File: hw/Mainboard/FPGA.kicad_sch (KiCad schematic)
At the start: 60 parts, among them J5 PMOD1, J6 PMOD2, J7 PROG, J8 FPGA_MCU, J9 BUS_EXPANSION, Q1 MMBT3904, SW3 CONFIG, U10 T8Q144C3

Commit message: hw: routing (wip)
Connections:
- net A2: now also U10.67 (GPIOB_RXP10); no longer U10.68 (GPIOB_RXN10)
- net I2C0_SCL: now also U10.15 (GPIOL_24_CLK0); no longer U10.14 (GPIOL_25_CLK1)
- net I2C0_SDA: now also U10.18 (GPIOL_20_CTRL0_CDI4); no longer U10.17 (GPIOL_21_CTRL1_CDI5)
- net I2C1_SCL: now also U10.14 (GPIOL_25_CLK1); no longer U10.15 (GPIOL_24_CLK0)
- net I2C1_SDA: now also U10.17 (GPIOL_21_CTRL1_CDI5); no longer U10.18 (GPIOL_20_CTRL0_CDI4)
- net RAM_A15: now also U10.68 (GPIOB_RXN10); no longer U10.67 (GPIOB_RXP10)
- net RDY: now also U10.43 (GPIOB_TXN04); no longer U10.45 (GPIOB_TXP06)
- net ~{SO}: now also U10.45 (GPIOB_TXP06); no longer U10.43 (GPIOB_TXN04)
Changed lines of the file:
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@@
     (effects (font (size 1.27 1.27)) (justify right bottom))
   )
-  (label "A2" (at 149.86 189.23 180)
-    (effects (font (size 1.27 1.27)) (justify right bottom))
+  (label "A2" (at 208.28 186.69 0)
+    (effects (font (size 1.27 1.27)) (justify left bottom))
   )
   (label "BE" (at 154.94 157.48 180)
@@
     (effects (font (size 1.27 1.27)) (justify left bottom))
   )
-  (label "RDY" (at 205.74 149.86 0)
-    (effects (font (size 1.27 1.27)) (justify left bottom))
+  (label "RDY" (at 154.94 152.4 180)
+    (effects (font (size 1.27 1.27)) (justify right bottom))
   )
   (label "A14" (at 389.89 93.98 0)
@@
     (effects (font (size 1.27 1.27)) (justify left bottom))
   )
-  (label "RAM_A15" (at 208.28 186.69 0)
-    (effects (font (size 1.27 1.27)) (justify left bottom))
+  (label "RAM_A15" (at 149.86 189.23 180)
+    (effects (font (size 1.27 1.27)) (justify right bottom))
   )
   (label "PMOD1_3" (at 311.15 2.54 180)
@@
     (effects (font (size 1.27 1.27)) (justify left bottom))
   )
-  (label "~{SO}" (at 154.94 152.4 180)
-    (effects (font (size 1.27 1.27)) (justify right bottom))
+  (label "~{SO}" (at 205.74 149.86 0)
+    (effects (font (size 1.27 1.27)) (justify left bottom))
   )
   (label "RAM_A11" (at 314.96 113.03 0)
@@
     (effects (font (size 1.27 1.27)) (justify right))
   )
-  (hierarchical_label "I2C1_SDA" (shape bidirectional) (at 149.86 127 180)
+  (hierarchical_label "I2C1_SDA" (shape bidirectional) (at 149.86 129.54 180)
     (effects (font (size 1.27 1.27)) (justify right))
   )
@@
     (effects (font (size 1.27 1.27)) (justify right))
   )
-  (hierarchical_label "I2C0_SDA" (shape bidirectional) (at 149.86 129.54 180)
+  (hierarchical_label "I2C0_SDA" (shape bidirectional) (at 149.86 127 180)
     (effects (font (size 1.27 1.27)) (justify right))
   )
@@
     (effects (font (size 1.27 1.27)) (justify right))
   )
-  (hierarchical_label "I2C0_SCL" (shape input) (at 210.82 127 0)
+  (hierarchical_label "I2C0_SCL" (shape input) (at 210.82 124.46 0)
     (effects (font (size 1.27 1.27)) (justify left))
   )
@@
     (effects (font (size 1.27 1.27)) (justify left))
   )
-  (hierarchical_label "I2C1_SCL" (shape input) (at 210.82 124.46 0)
-    (effects (font (size 1.27 1.27)) (justify left))
-  )
+  (hierarchical_label "I2C1_SCL" (shape input) (at 210.82 127 0)
+    (effects (font (size 1.27 1.27)) (justify left))
+  )

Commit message: hw: header_and_jumper, button for flashing (wip)
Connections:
- net GND: now also J8.14 (Pin_14)
- net PMOD2_1: now also U10.139 (GPIOL_68); no longer U10.138 (GPIOL_69_CBSEL1)
- net PMOD2_5: now also U10.138 (GPIOL_69_CBSEL1); no longer U10.139 (GPIOL_68)
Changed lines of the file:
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@@
     (stroke (width 0) (type default) (color 0 0 0 0))
   )
+  (wire (pts (xy 226.06 43.18) (xy 217.17 43.18))
+    (stroke (width 0) (type default) (color 0 0 0 0))
+  )
   (wire (pts (xy 95.25 160.02) (xy 95.25 162.56))
     (stroke (width 0) (type default) (color 0 0 0 0))
@@
     (stroke (width 0) (type default) (color 0 0 0 0))
   )
+  (wire (pts (xy 217.17 58.42) (xy 226.06 58.42))
+    (stroke (width 0) (type default) (color 0 0 0 0))
+  )
   (wire (pts (xy 53.34 29.21) (xy 55.88 29.21))
     (stroke (width 0) (type default) (color 0 0 0 0))
@@
     (effects (font (size 1.27 1.27)) (justify left bottom))
   )
-  (label "PMOD2_1" (at 242.57 203.2 180)
+  (label "PMOD2_1" (at 242.57 200.66 180)
     (effects (font (size 1.27 1.27)) (justify right bottom))
   )
@@
     (effects (font (size 1.27 1.27)) (justify left bottom))
   )
-  (label "PMOD2_5" (at 242.57 200.66 180)
+  (label "PMOD2_5" (at 242.57 203.2 180)
     (effects (font (size 1.27 1.27)) (justify right bottom))
   )
@@
       (effects (font (size 1.27 1.27)) hide)
     )
-    (property "Value" "GND" (id 1) (at 187.96 43.18 0))
+    (property "Value" "GND" (id 1) (at 187.96 43.18 90))
     (property "Footprint" "" (id 2) (at 193.04 43.18 0)
       (effects (font (size 1.27 1.27)) hide)
@@
     (pin "1")
   )
-  (symbol (lib_id "power:+3V3") (at 217.17 43.18 270) (mirror x) (unit 1)
+  (symbol (lib_id "power:+3V3") (at 226.06 43.18 270) (mirror x) (unit 1)
     (in_bom yes) (on_board yes)
-    (property "Reference" "#PWR068" (id 0) (at 213.36 43.18 0)
+    (property "Reference" "#PWR068" (id 0) (at 222.25 43.18 0)
       (effects (font (size 1.27 1.27)) hide)
     )
-    (property "Value" "+3V3" (id 1) (at 223.52 43.18 90))
-    (property "Footprint" "" (id 2) (at 217.17 43.18 0)
+    (property "Value" "+3V3" (id 1) (at 232.41 43.18 90))
+    (property "Footprint" "" (id 2) (at 226.06 43.18 0)
       (effects (font (size 1.27 1.27)) hide)
     )
-    (property "Datasheet" "" (id 3) (at 217.17 43.18 0)
+    (property "Datasheet" "" (id 3) (at 226.06 43.18 0)
       (effects (font (size 1.27 1.27)) hide)
     )
@@
     (pin "1")
   )
+  (symbol (lib_id "power:GND") (at 226.06 58.42 90) (mirror x) (unit 1)
+    (in_bom yes) (on_board yes)
+    (property "Reference" "#PWR0174" (id 0) (at 232.41 58.42 0)
+      (effects (font (size 1.27 1.27)) hide)
+    )
+    (property "Value" "GND" (id 1) (at 231.14 58.42 90))
+    (property "Footprint" "" (id 2) (at 226.06 58.42 0)
+      (effects (font (size 1.27 1.27)) hide)
+    )
+    (property "Datasheet" "" (id 3) (at 226.06 58.42 0)
+      (effects (font (size 1.27 1.27)) hide)
+    )
+    (pin "1")
+  )
   (symbol (lib_id "Device:R_Pack04") (at 317.5 86.36 270) (mirror x) (unit 1)
     (in_bom yes) (on_board yes)
@@
       (effects (font (size 1.27 1.27)) hide)
     )
-    (property "Value" "GND" (id 1) (at 187.96 58.42 0))
+    (property "Value" "GND" (id 1) (at 187.96 58.42 90))
     (property "Footprint" "" (id 2) (at 193.04 58.42 0)
       (effects (font (size 1.27 1.27)) hide)

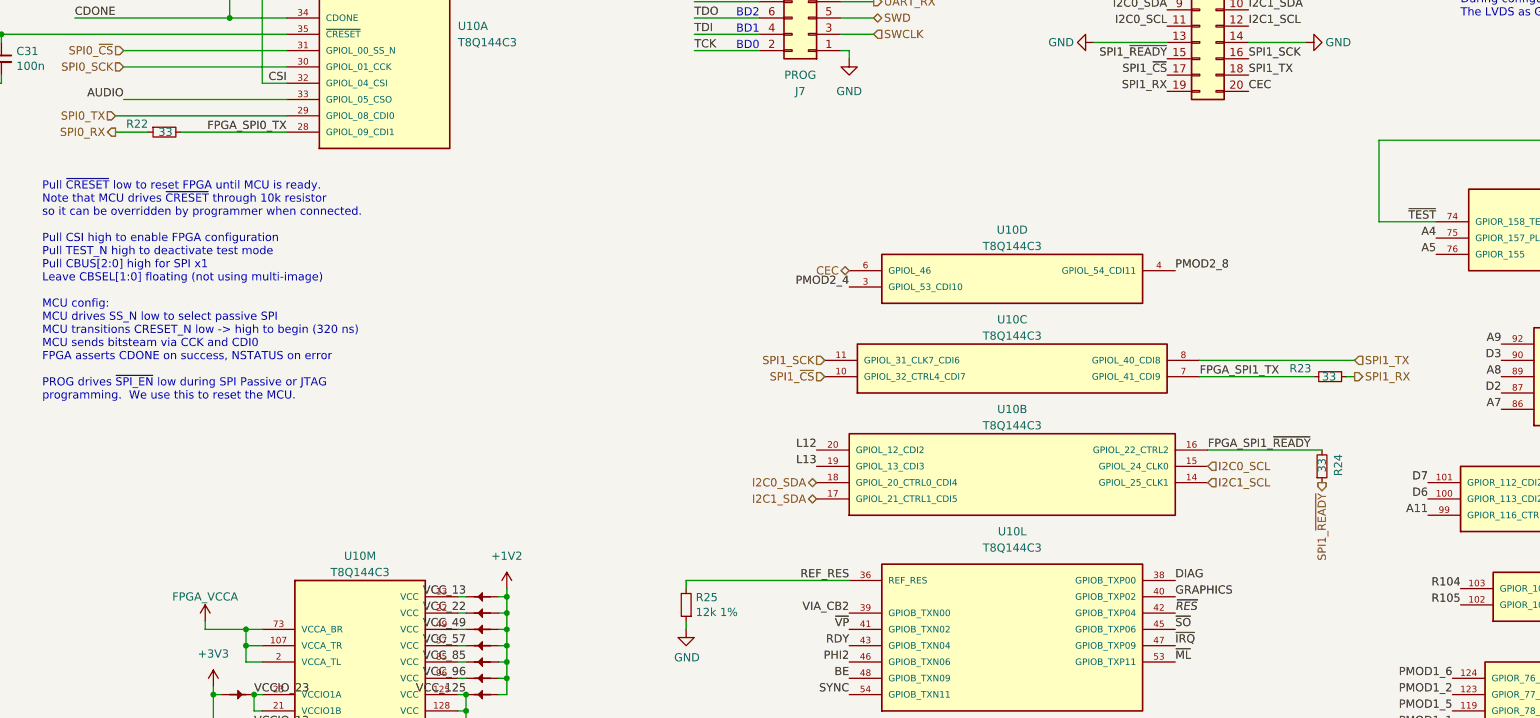
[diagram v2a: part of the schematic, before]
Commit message: hw: remove series termination, gnd under hdmi (wip)
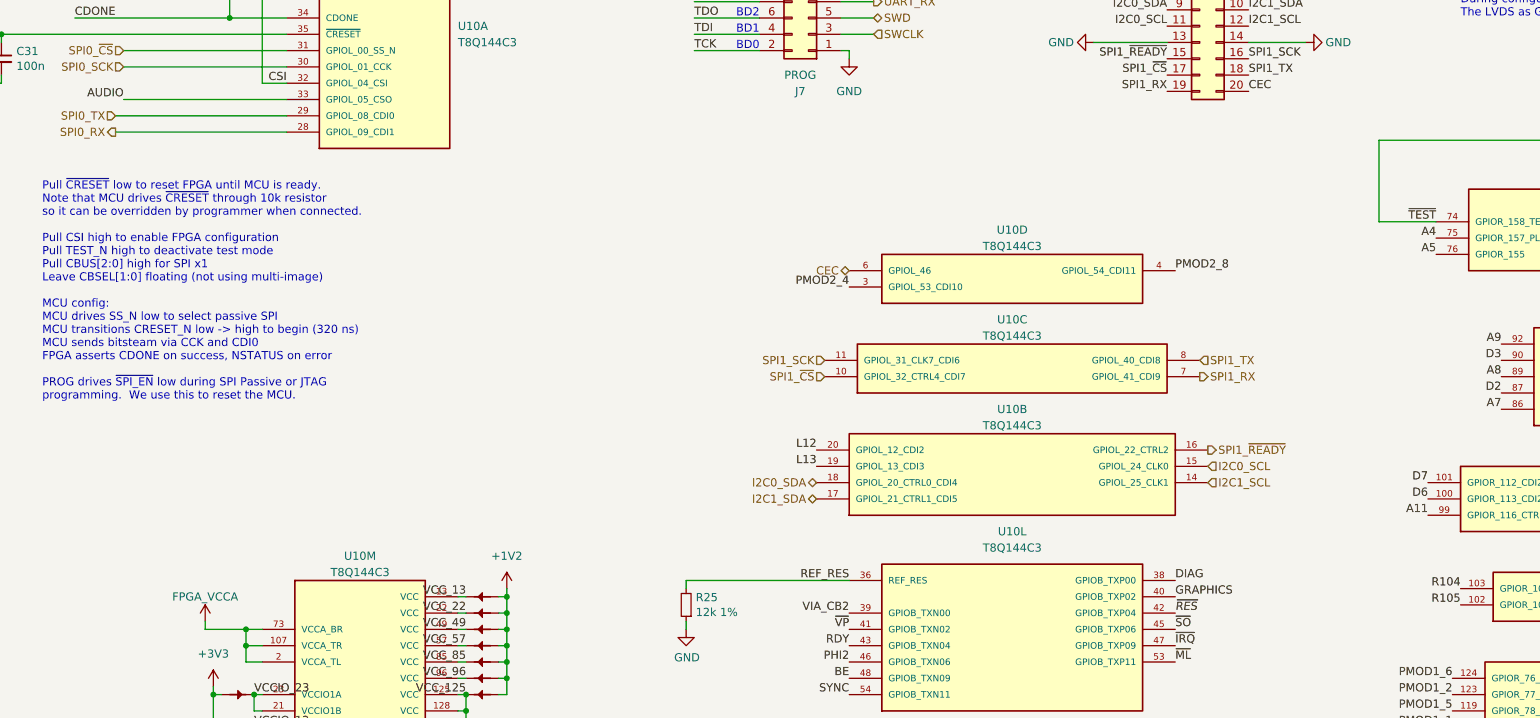
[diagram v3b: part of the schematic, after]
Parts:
- removed R22, R23, R24: 33, Resistor_SMD:R_0402_1005Metric, symbol Device:R_Small
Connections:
- net FPGA_SPI0_TX is gone; now on net SPI0_RX: U10.28 (GPIOL_09_CDI1)
- net FPGA_SPI1_TX is gone; now on net SPI1_RX: U10.7 (GPIOL_41_CDI9)
- net FPGA_SPI1_~{READY} is gone; now on net SPI1_~{READY}: U10.16 (GPIOL_22_CTRL2)
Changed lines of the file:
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@@
     (stroke (width 0) (type default) (color 0 0 0 0))
   )
-  (wire (pts (xy 50.8 72.39) (xy 67.31 72.39))
+  (wire (pts (xy 40.64 72.39) (xy 67.31 72.39))
     (stroke (width 0) (type default) (color 0 0 0 0))
   )
@@
     (stroke (width 0) (type default) (color 0 0 0 0))
   )
-  (wire (pts (xy 228.6 121.92) (xy 210.82 121.92))
-    (stroke (width 0) (type default) (color 0 0 0 0))
-  )
   (bus (pts (xy 365.76 106.68) (xy 365.76 109.22))
     (stroke (width 0) (type default) (color 0 0 0 0))
@@
     (stroke (width 0) (type default) (color 0 0 0 0))
   )
-  (wire (pts (xy 233.68 107.95) (xy 209.55 107.95))
-    (stroke (width 0) (type default) (color 0 0 0 0))
-  )
   (wire (pts (xy 138.43 251.46) (xy 138.43 252.73))
     (stroke (width 0) (type default) (color 0 0 0 0))
@@
     (stroke (width 0) (type default) (color 0 0 0 0))
   )
-  (wire (pts (xy 40.64 72.39) (xy 45.72 72.39))
-    (stroke (width 0) (type default) (color 0 0 0 0))
-  )
   (wire (pts (xy 62.23 180.34) (xy 63.5 180.34))
     (stroke (width 0) (type default) (color 0 0 0 0))
@@
     (stroke (width 0) (type default) (color 0 0 0 0))
   )
-  (wire (pts (xy 209.55 110.49) (xy 227.33 110.49))
-    (stroke (width 0) (type default) (color 0 0 0 0))
-  )
   (bus (pts (xy 365.76 111.76) (xy 365.76 116.84))
     (stroke (width 0) (type default) (color 0 0 0 0))
@@
     (stroke (width 0) (type default) (color 0 0 0 0))
   )
-  (wire (pts (xy 232.41 110.49) (xy 233.68 110.49))
-    (stroke (width 0) (type default) (color 0 0 0 0))
-  )
   (wire (pts (xy 50.8 29.21) (xy 50.8 30.48))
     (stroke (width 0) (type default) (color 0 0 0 0))
@@
     (effects (font (size 1.27 1.27)) (justify left bottom))
   )
-  (label "FPGA_SPI1_~{READY}" (at 210.82 121.92 0)
-    (effects (font (size 1.27 1.27)) (justify left bottom))
-  )
   (label "PMOD1_8" (at 303.53 190.5 0)
     (effects (font (size 1.27 1.27)) (justify left bottom))
@@
     (effects (font (size 1.27 1.27)) (justify left bottom))
   )
-  (label "FPGA_SPI0_TX" (at 67.31 72.39 180)
-    (effects (font (size 1.27 1.27)) (justify right bottom))
-  )
   (label "A10" (at 311.15 129.54 0)
     (effects (font (size 1.27 1.27)) (justify left bottom))
@@
     (effects (font (size 1.27 1.27)) (justify right bottom))
   )
-  (label "FPGA_SPI1_TX" (at 209.55 110.49 0)
-    (effects (font (size 1.27 1.27)) (justify left bottom))
-  )
   (label "VCC_96" (at 95.25 157.48 180)
     (effects (font (size 1.27 1.27)) (justify right bottom))
@@
     (effects (font (size 1.27 1.27)) (justify left))
   )
-  (hierarchical_label "SPI1_TX" (shape input) (at 233.68 107.95 0)
+  (hierarchical_label "SPI1_TX" (shape input) (at 209.55 107.95 0)
     (effects (font (size 1.27 1.27)) (justify left))
   )
-  (hierarchical_label "SPI1_RX" (shape output) (at 233.68 110.49 0)
+  (hierarchical_label "SPI1_RX" (shape output) (at 209.55 110.49 0)
     (effects (font (size 1.27 1.27)) (justify left))
   )
@@
     (effects (font (size 1.27 1.27)) (justify left))
   )
-  (hierarchical_label "SPI1_~{READY}" (shape output) (at 228.6 127 270)
-    (effects (font (size 1.27 1.27)) (justify right))
+  (hierarchical_label "SPI1_~{READY}" (shape output) (at 210.82 121.92 0)
+    (effects (font (size 1.27 1.27)) (justify left))
   )
   (hierarchical_label "SPI0_SCK" (shape input) (at 41.91 62.23 180)
@@
     (pin "2")
   )
-  (symbol (lib_id "Device:R_Small") (at 228.6 124.46 0) (mirror x) (unit 1)
-    (in_bom yes) (on_board yes)
-    (property "Reference" "R24" (id 0) (at 231.14 122.555 90)
-      (effects (font (size 1.27 1.27)) (justify left))
-    )
-    (property "Value" "33" (id 1) (at 228.6 123.19 90)
-      (effects (font (size 1.27 1.27)) (justify left))
-    )
-    (property "Footprint" "Resistor_SMD:R_0402_1005Metric" (id 2) (at 228.6 124.46 0)
-      (effects (font (size 1.27 1.27)) hide)
-    )
-    (property "Datasheet" "https://datasheet.lcsc.com/lcsc/2205311900_UNI-ROYAL-Uniroyal-Elec-0402WGF330JTCE_C25105.pdf" (id 3) (at 228.6 124.46 0)
-      (effects (font (size 1.27 1.27)) hide)
-    )
-    (property "LCSC" "C25105" (id 4) (at 228.6 124.46 0)
-      (effects (font (size 1.27 1.27)) hide)
-    )
-    (pin "1")
-    (pin "2")
-  )
   (symbol (lib_id "Device:R_Small") (at 63.5 35.56 0) (mirror x) (unit 1)
     (in_bom yes) (on_board yes)
@@
     (pin "1")
   )
-  (symbol (lib_id "Device:R_Small") (at 229.87 110.49 270) (unit 1)
-    (in_bom yes) (on_board yes)
-    (property "Reference" "R23" (id 0) (at 223.52 109.22 90)
-      (effects (font (size 1.27 1.27)) (justify left))
-    )
-    (property "Value" "33" (id 1) (at 228.6 110.49 90)
-      (effects (font (size 1.27 1.27)) (justify left))
-    )
-    (property "Footprint" "Resistor_SMD:R_0402_1005Metric" (id 2) (at 229.87 110.49 0)
-      (effects (font (size 1.27 1.27)) hide)
-    )
-    (property "Datasheet" "https://datasheet.lcsc.com/lcsc/2205311900_UNI-ROYAL-Uniroyal-Elec-0402WGF330JTCE_C25105.pdf" (id 3) (at 229.87 110.49 0)
-      (effects (font (size 1.27 1.27)) hide)
-    )
-    (property "LCSC" "C25105" (id 4) (at 229.87 110.49 0)
-      (effects (font (size 1.27 1.27)) hide)
-    )
-    (pin "1")
-    (pin "2")
-  )
   (symbol (lib_id "power:GND") (at 193.04 43.18 270) (unit 1)
     (in_bom yes) (on_board yes)
@@
     (pin "96")
   )
-  (symbol (lib_id "Device:R_Small") (at 48.26 72.39 90) (mirror x) (unit 1)
-    (in_bom yes) (on_board yes)
-    (property "Reference" "R22" (id 0) (at 45.72 71.12 90)
-      (effects (font (size 1.27 1.27)) (justify left))
-    )
-    (property "Value" "33" (id 1) (at 49.53 72.39 90)
-      (effects (font (size 1.27 1.27)) (justify left))
-    )
-    (property "Footprint" "Resistor_SMD:R_0402_1005Metric" (id 2) (at 48.26 72.39 0)
-      (effects (font (size 1.27 1.27)) hide)
-    )
-    (property "Datasheet" "https://datasheet.lcsc.com/lcsc/2205311900_UNI-ROYAL-Uniroyal-Elec-0402WGF330JTCE_C25105.pdf" (id 3) (at 48.26 72.39 0)
-      (effects (font (size 1.27 1.27)) hide)
-    )
-    (property "LCSC" "C25105" (id 4) (at 48.26 72.39 0)
-      (effects (font (size 1.27 1.27)) hide)
-    )
-    (pin "1")
-    (pin "2")
-  )
   (symbol (lib_id "PET:PowerTie_2") (at 59.69 185.42 0) (mirror x) (unit 1)

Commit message: hw: fill, routing, and silk touchups (wip)
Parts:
- added C92, C94: 1u, Capacitor_SMD:C_0402_1005Metric, symbol Device:C_Small
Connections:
- net VSS is gone; now on net GND: PT30.2, U10.1 (GND), U10.104 (GND), U10.108 (GND), U10.120 (GND), U10.121 (GND), U10.126 (GND), U10.127 (GND), U10.129 (GND), U10.133 (GND), U10.37 (GND), U10.44 (GND), U10.5 (GND), U10.50 (GND), U10.64 (GND), U10.9 (GND), U10.94 (GND)
- net +3V3: now also C92.1, C94.1
- net PD_GND: now also C92.2, C94.2
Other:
- moved on the sheet: J6
